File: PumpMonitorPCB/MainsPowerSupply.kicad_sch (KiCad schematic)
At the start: 17 parts, among them J2 Mains terminals, K2 J115F11CH5VDCS61-5U Relay, Q2 AS2302, U5 ACS770xCB-050B-PFF, U6 AMS1117-3.3

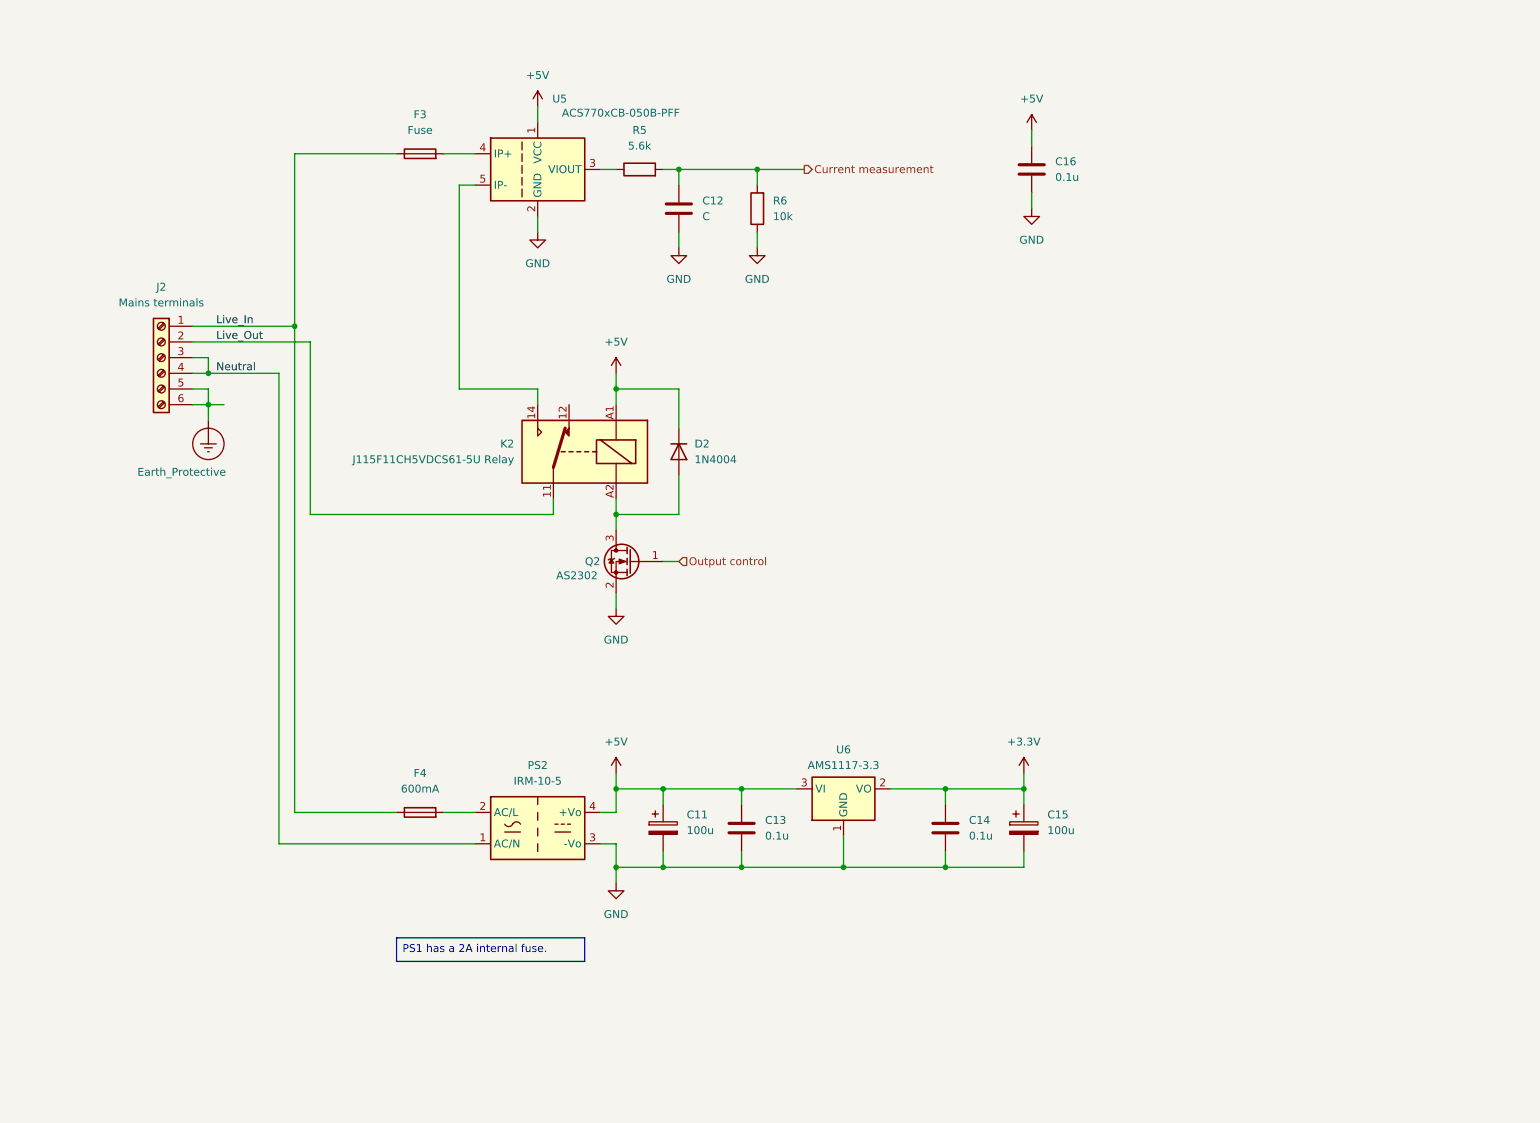
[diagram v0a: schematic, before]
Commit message: Adding microcontroller, USB, UI components.
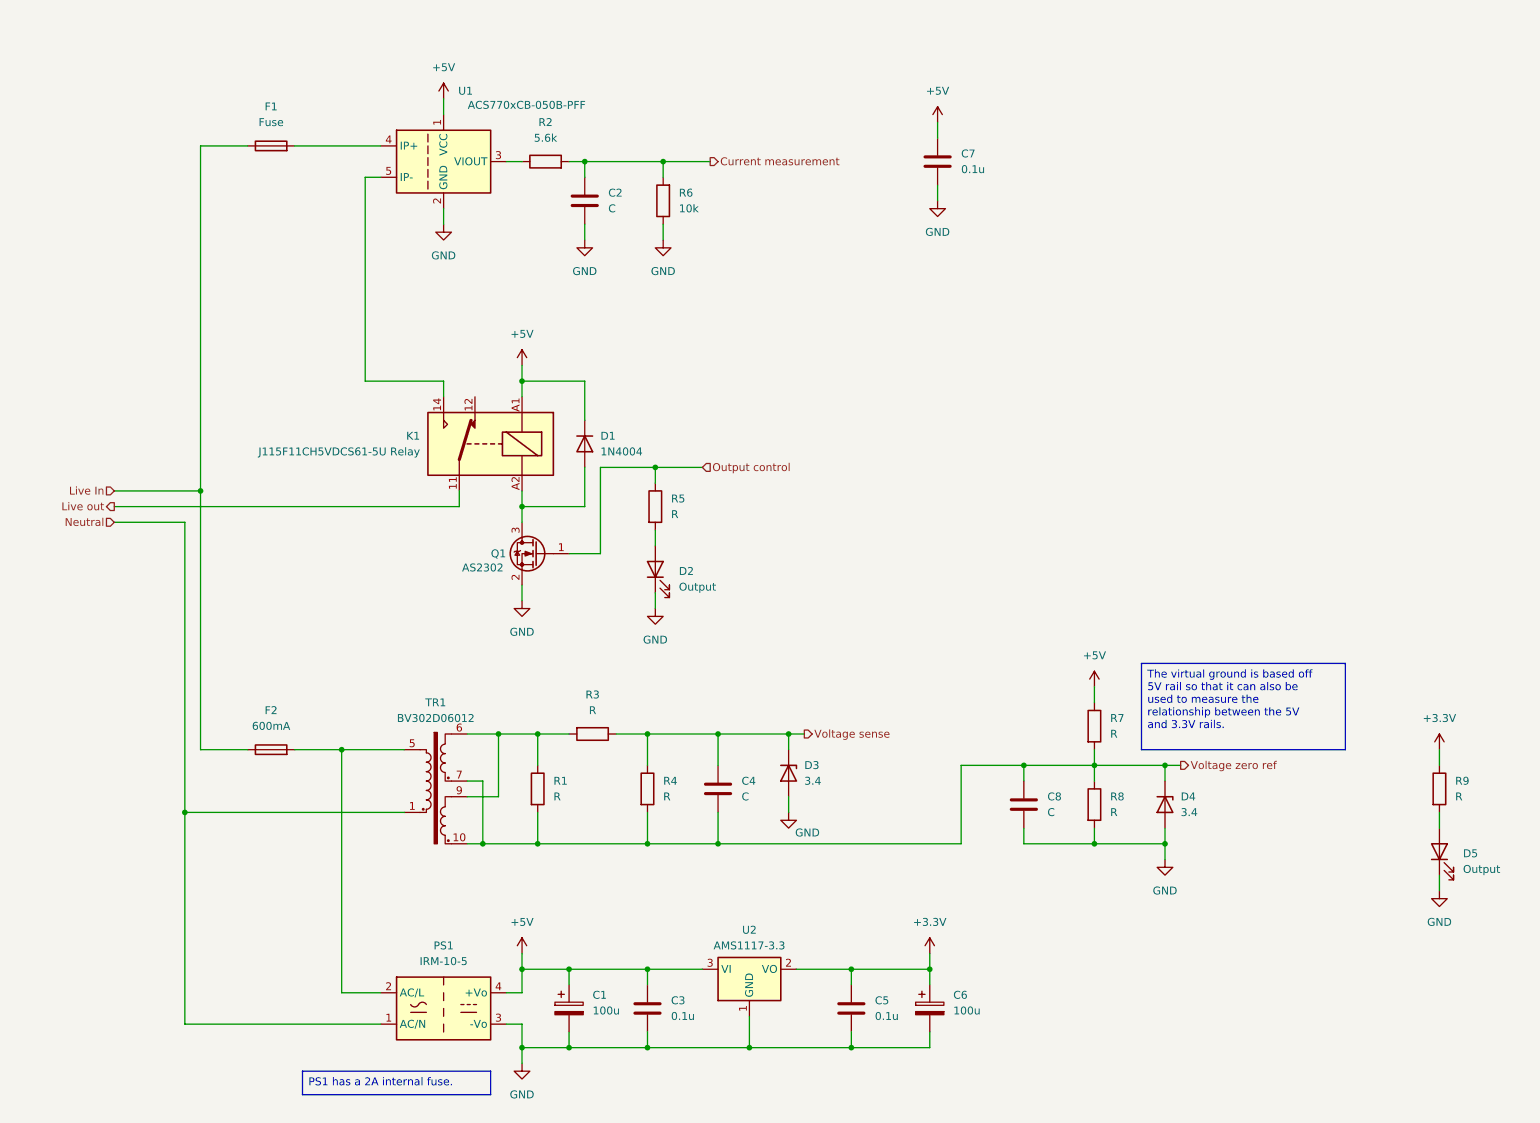
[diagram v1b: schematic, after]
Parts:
- removed J2: Mains terminals, symbol Connector:Screw_Terminal_01x06
- added C4, C8: C, symbol Device:C
- added D2, D5: Output, symbol Device:LED
- added D3, D4: 3.4, symbol Device:D_Zener
- added R1, R3, R4, R5, R7, R8, R9: R, symbol Device:R
- added TR1: BV302D06012, symbol PumpMonitorCustom:BV302D06012
- renumbered C11 to C1, C12 to C2, C13 to C3, C14 to C5, C15 to C6, C16 to C7, D2 to D1, F3 to F1, F4 to F2, K2 to K1, PS2 to PS1, Q2 to Q1, R5 to R2, U5 to U1, U6 to U2
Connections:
- net +3.3V: now also R9.1
- net +5V: now also R7.1
- net GND: now also C8.2, D2.1 (K), D3.2 (A), D4.2 (A), D5.1 (K), R8.2
- net Neutral: now also TR1.1
- net Output control: now also R5.1
- net at F2.2, PS1.2 (AC/L): now also TR1.5
- net Live_In renamed Live In
- net Live_Out renamed Live out
- new net: R1.1, R3.2, TR1.6, TR1.9
- new net: D2.2 (A), R5.2
- new net: D5.2 (A), R9.2
- new net Voltage sense: C4.1, D3.1 (K), R3.1, R4.1
- new net Voltage zero ref: C4.2, C8.1, D4.1 (K), R1.2, R4.2, R7.2, R8.1, TR1.10, TR1.7
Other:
- title: Pump monitor: mains wiring and power supply -> Pump monitor - mains and power supply
- moved on the sheet: C1, C2, C3, C5, C6, C7, D1, F1, F2, K1, PS1, Q1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

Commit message: Tidied schematic, added LoRa module.
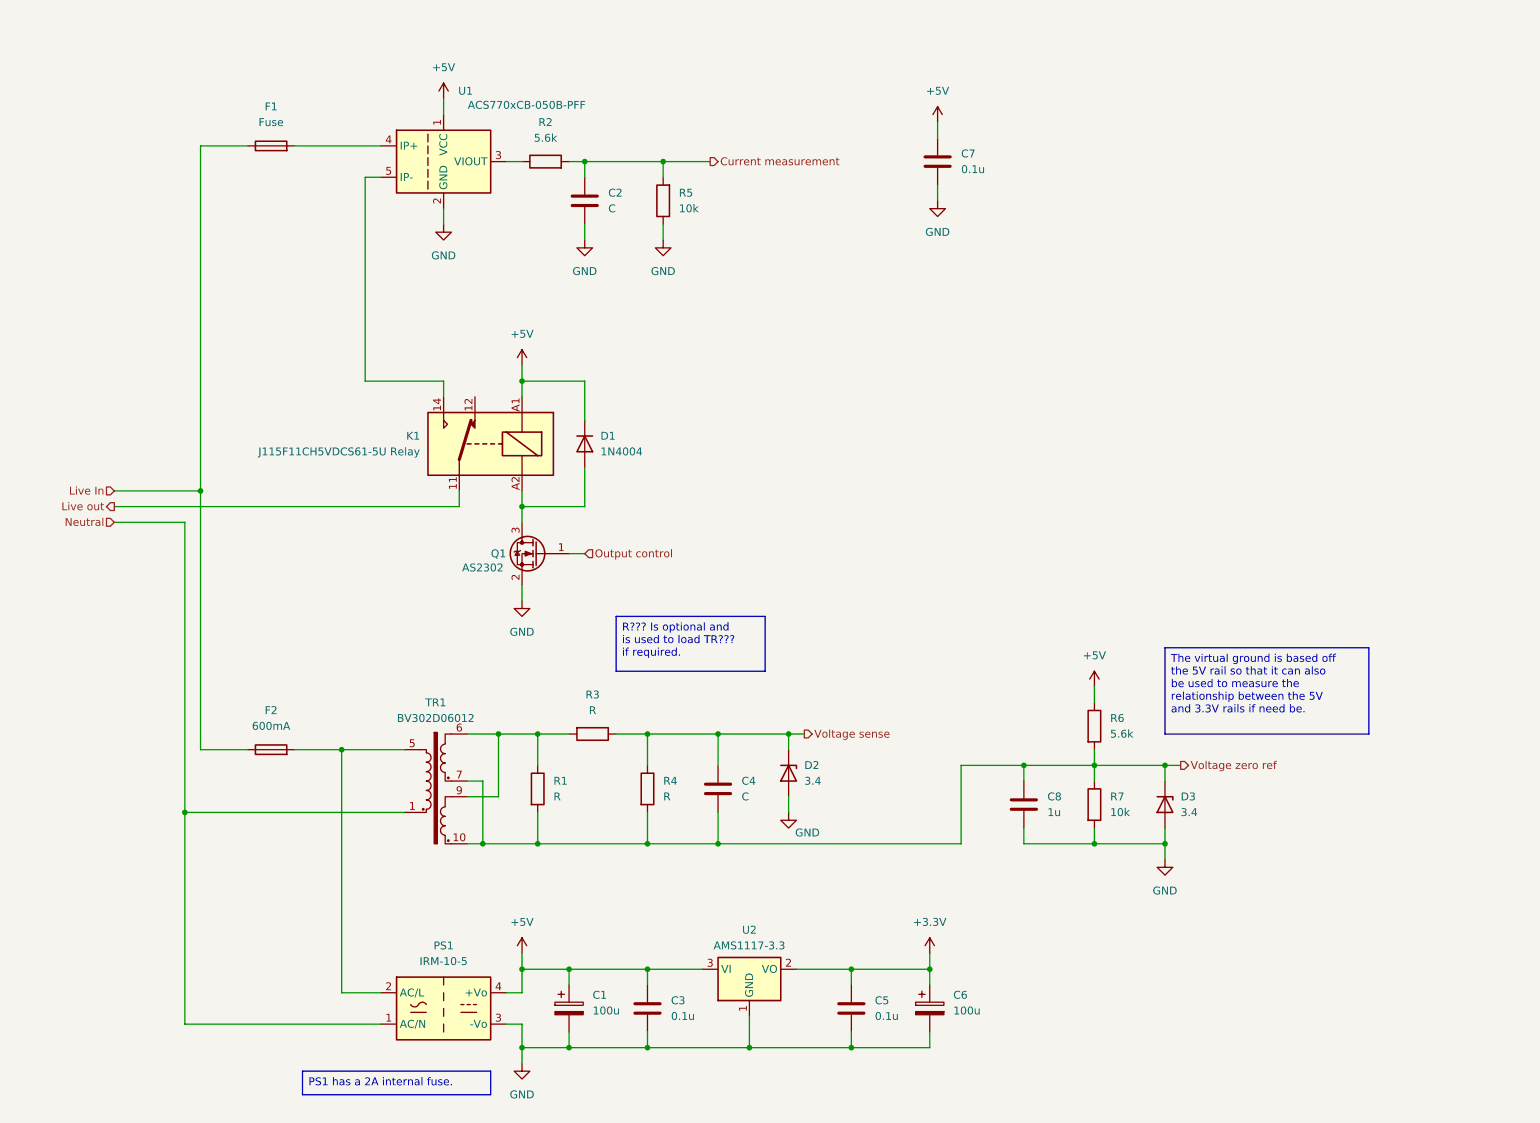
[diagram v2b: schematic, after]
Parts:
- removed D2, D5: Output, symbol Device:LED
- removed R5, R9: R, symbol Device:R
- C8: value C -> 1u
- R6: renamed from R7; value R -> 5.6k
- R7: renamed from R8; value R -> 10k
- renumbered D3 to D2, D4 to D3, R6 to R5

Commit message: Added aux. connectors, started assigning components.
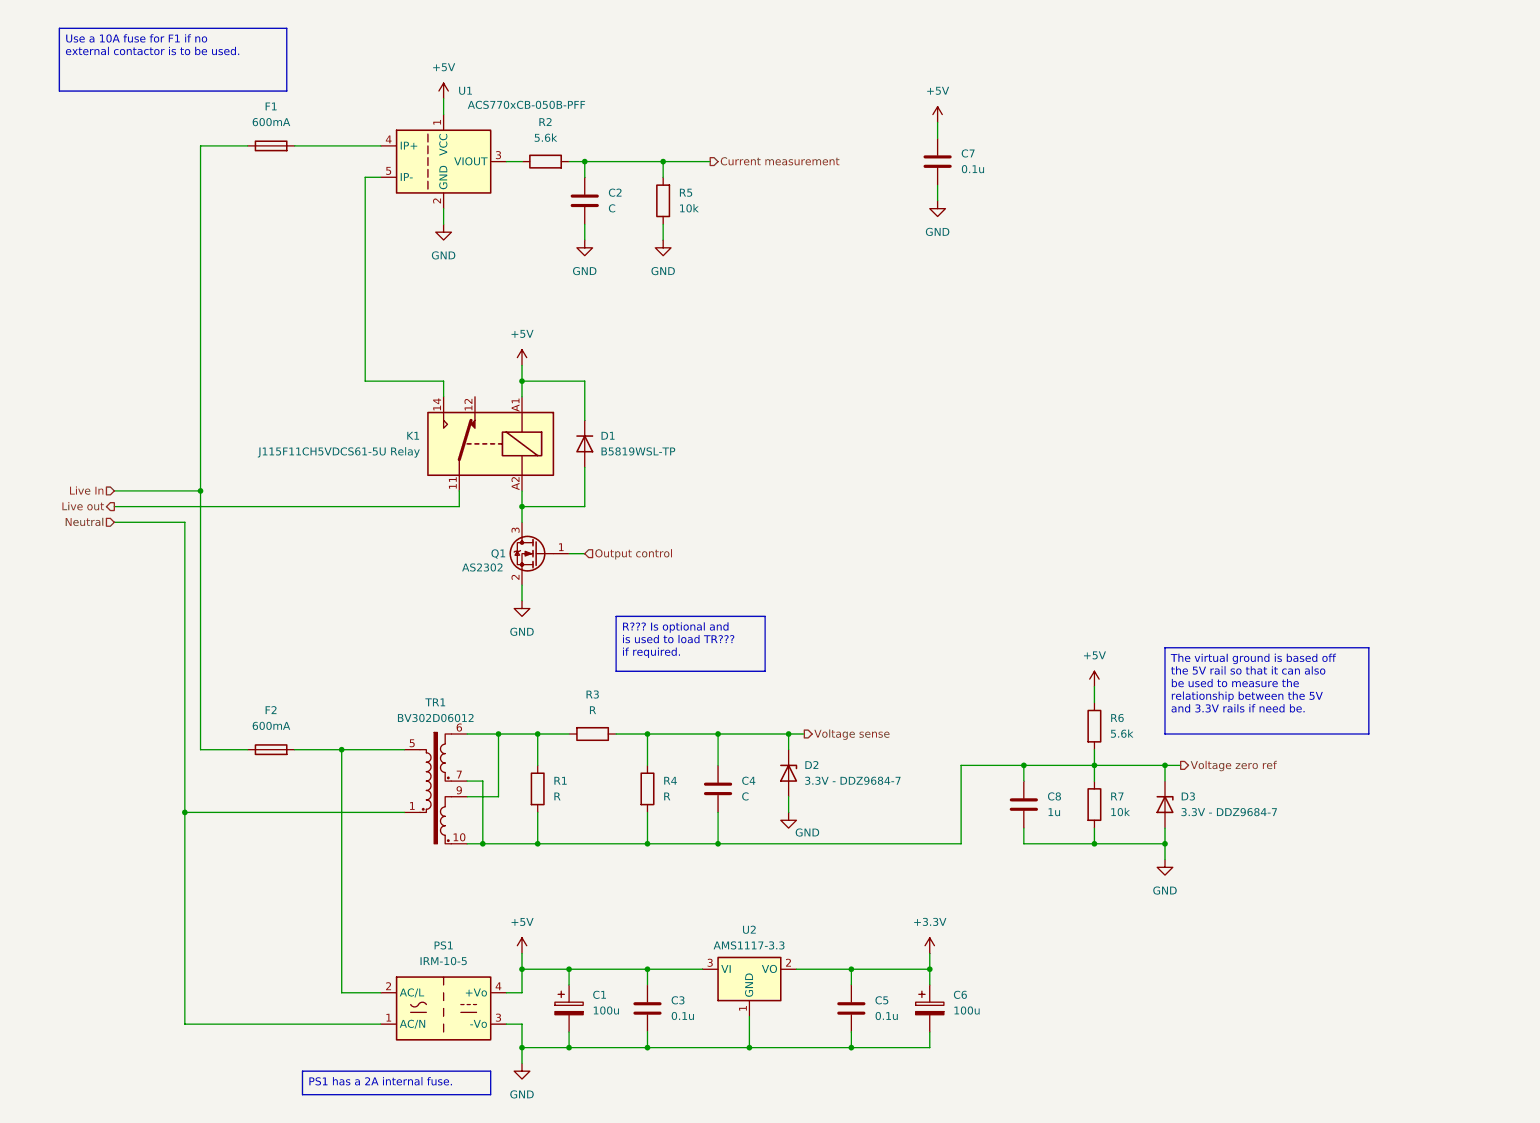
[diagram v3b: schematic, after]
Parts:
- C1, C6: footprint (none) -> Capacitor_THT:CP_Radial_D10.0mm_P3.80mm
- C2, C3, C4, C5, C7, C8: footprint (none) -> Capacitor_SMD:C_0805_2012Metric_Pad1.18x1.45mm_HandSolder
- D1: value 1N4004 -> B5819WSL-TP; footprint Diode_THT:D_DO-41_SOD81_P10.16mm_Horizontal -> Diode_SMD:D_SOD-323F
- D2, D3: value 3.4 -> 3.3V - DDZ9684-7; footprint (none) -> Diode_SMD:D_SOD-123F
- F1: value Fuse -> 600mA
- R1: footprint (none) -> Resistor_THT:R_Axial_DIN0207_L6.3mm_D2.5mm_P7.62mm_Horizontal
- R2, R3, R4, R5, R6, R7: footprint (none) -> Resistor_SMD:R_0805_2012Metric_Pad1.20x1.40mm_HandSolder
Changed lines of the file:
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@@
 		)
 	)
+	(text_box "Use a 10A fuse for F1 if no external contactor is to be used."
+		(exclude_from_sim no)
+		(at 17.78 15.24 0)
+		(size 36.83 10.16)
+		(margins 0.9525 0.9525 0.9525 0.9525)
+		(stroke
+			(width 0)
+			(type solid)
+		)
+		(fill
+			(type none)
+		)
+		(effects
+			(font
+				(size 1.27 1.27)
+			)
+			(justify left top)
+		)
+	)
 	(junction
 		(at 92.71 92.71)
@@
 			)
 		)
-		(property "Footprint" ""
+		(property "Footprint" "Capacitor_SMD:C_0805_2012Metric_Pad1.18x1.45mm_HandSolder"
 			(at 125.4252 142.24 0)
 			(effects
@@
 			)
 		)
-		(property "Footprint" ""
+		(property "Footprint" "Resistor_SMD:R_0805_2012Metric_Pad1.20x1.40mm_HandSolder"
 			(at 183.642 140.97 90)
 			(effects
@@
 			)
 		)
-		(property "Footprint" ""
+		(property "Footprint" "Resistor_SMD:R_0805_2012Metric_Pad1.20x1.40mm_HandSolder"
 			(at 117.348 43.18 90)
 			(effects
@@
 			)
 		)
-		(property "Footprint" ""
+		(property "Footprint" "Capacitor_THT:CP_Radial_D10.0mm_P3.80mm"
 			(at 159.7152 177.8 0)
 			(effects
@@
 			)
 		)
-		(property "Footprint" ""
+		(property "Footprint" "Capacitor_SMD:C_0805_2012Metric_Pad1.18x1.45mm_HandSolder"
 			(at 147.0152 177.8 0)
 			(effects
@@
 			)
 		)
-		(property "Footprint" ""
+		(property "Footprint" "Capacitor_SMD:C_0805_2012Metric_Pad1.18x1.45mm_HandSolder"
 			(at 174.9552 144.78 0)
 			(effects
@@
 			)
 		)
-		(property "Value" "3.4"
+		(property "Value" "3.3V - DDZ9684-7"
 			(at 138.43 137.1599 90)
 			(effects
@@
 			)
 		)
-		(property "Footprint" ""
+		(property "Footprint" "Diode_SMD:D_SOD-123F"
 			(at 135.89 135.89 0)
 			(effects
@@
 			)
 		)
-		(property "Value" "Fuse"
+		(property "Value" "600mA"
 			(at 52.07 30.48 90)
 			(effects
@@
 			)
 		)
-		(property "Footprint" ""
+		(property "Footprint" "Capacitor_SMD:C_0805_2012Metric_Pad1.18x1.45mm_HandSolder"
 			(at 160.9852 40.64 0)
 			(effects
@@
 			)
 		)
-		(property "Footprint" ""
+		(property "Footprint" "Resistor_THT:R_Axial_DIN0207_L6.3mm_D2.5mm_P7.62mm_Horizontal"
 			(at 93.472 138.43 90)
 			(effects
@@
 			)
 		)
-		(property "Footprint" ""
+		(property "Footprint" "Capacitor_SMD:C_0805_2012Metric_Pad1.18x1.45mm_HandSolder"
 			(at 113.9952 177.8 0)
 			(effects
@@
 			)
 		)
-		(property "Value" "3.4"
+		(property "Value" "3.3V - DDZ9684-7"
 			(at 199.39 142.2399 90)
 			(effects
@@
 			)
 		)
-		(property "Footprint" ""
+		(property "Footprint" "Diode_SMD:D_SOD-123F"
 			(at 196.85 140.97 0)
 			(effects
@@
 			)
 		)
-		(property "Footprint" ""
+		(property "Footprint" "Capacitor_SMD:C_0805_2012Metric_Pad1.18x1.45mm_HandSolder"
 			(at 103.8352 46.99 0)
 			(effects
@@
 			)
 		)
-		(property "Footprint" ""
+		(property "Footprint" "Resistor_SMD:R_0805_2012Metric_Pad1.20x1.40mm_HandSolder"
 			(at 96.52 38.608 90)
 			(effects
@@
 			)
 		)
-		(property "Footprint" ""
+		(property "Footprint" "Resistor_SMD:R_0805_2012Metric_Pad1.20x1.40mm_HandSolder"
 			(at 183.642 128.27 90)
 			(effects
@@
 			)
 		)
-		(property "Footprint" ""
+		(property "Footprint" "Resistor_SMD:R_0805_2012Metric_Pad1.20x1.40mm_HandSolder"
 			(at 104.14 127.762 90)
 			(effects
@@
 			)
 		)
-		(property "Footprint" ""
+		(property "Footprint" "Capacitor_THT:CP_Radial_D10.0mm_P3.80mm"
 			(at 101.2952 177.8 0)
 			(effects
@@
 			)
 		)
-		(property "Value" "1N4004"
+		(property "Value" "B5819WSL-TP"
 			(at 105.41 83.8199 90)
 			(effects
@@
 			)
 		)
-		(property "Footprint" "Diode_THT:D_DO-41_SOD81_P10.16mm_Horizontal"
+		(property "Footprint" "Diode_SMD:D_SOD-323F"
 			(at 98.425 82.55 0)
 			(effects
@@
 			)
 		)
-		(property "Footprint" ""
+		(property "Footprint" "Resistor_SMD:R_0805_2012Metric_Pad1.20x1.40mm_HandSolder"
 			(at 111.252 138.43 90)
 			(effects
